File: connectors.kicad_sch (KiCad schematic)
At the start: 2 parts

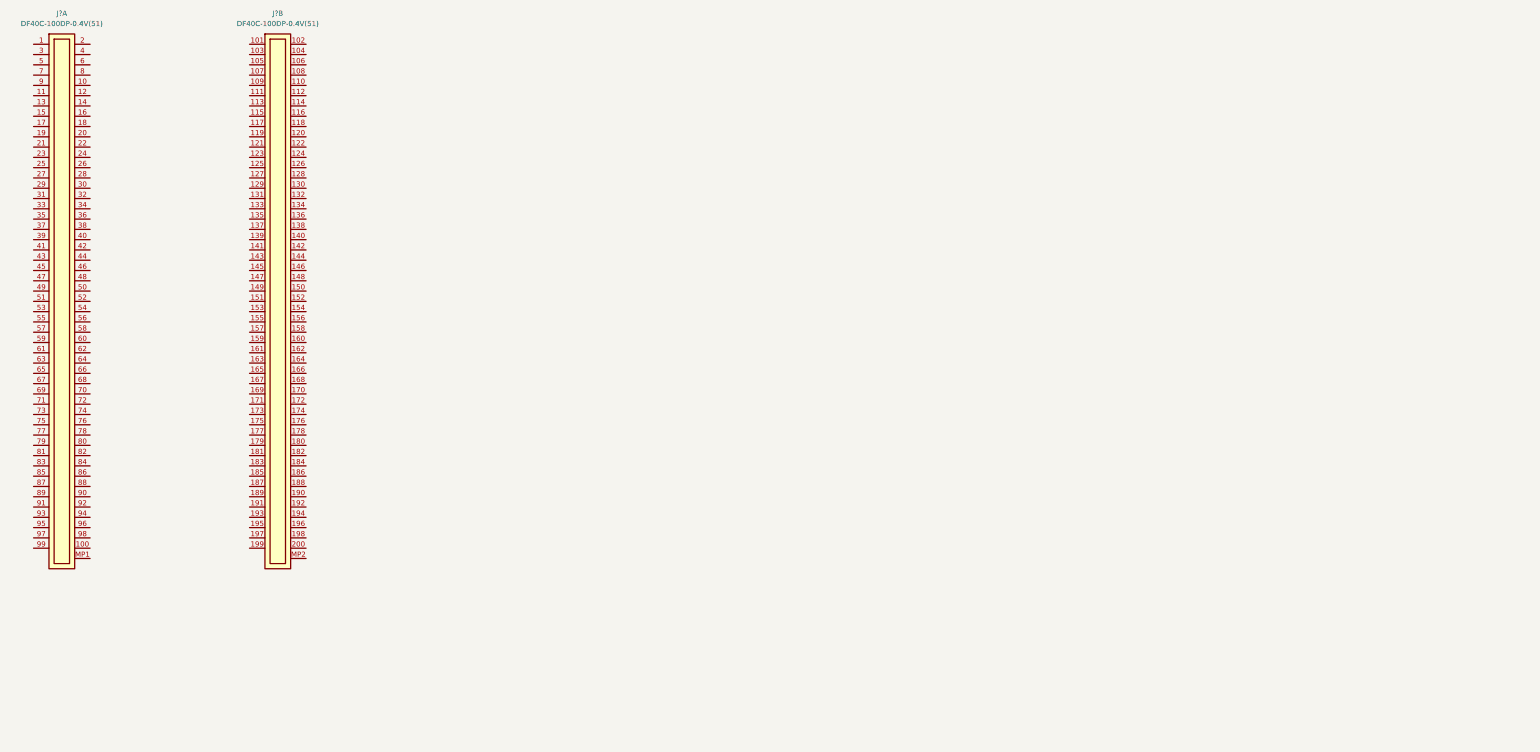
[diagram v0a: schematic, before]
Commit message: [#52579] Connect signals to SoC
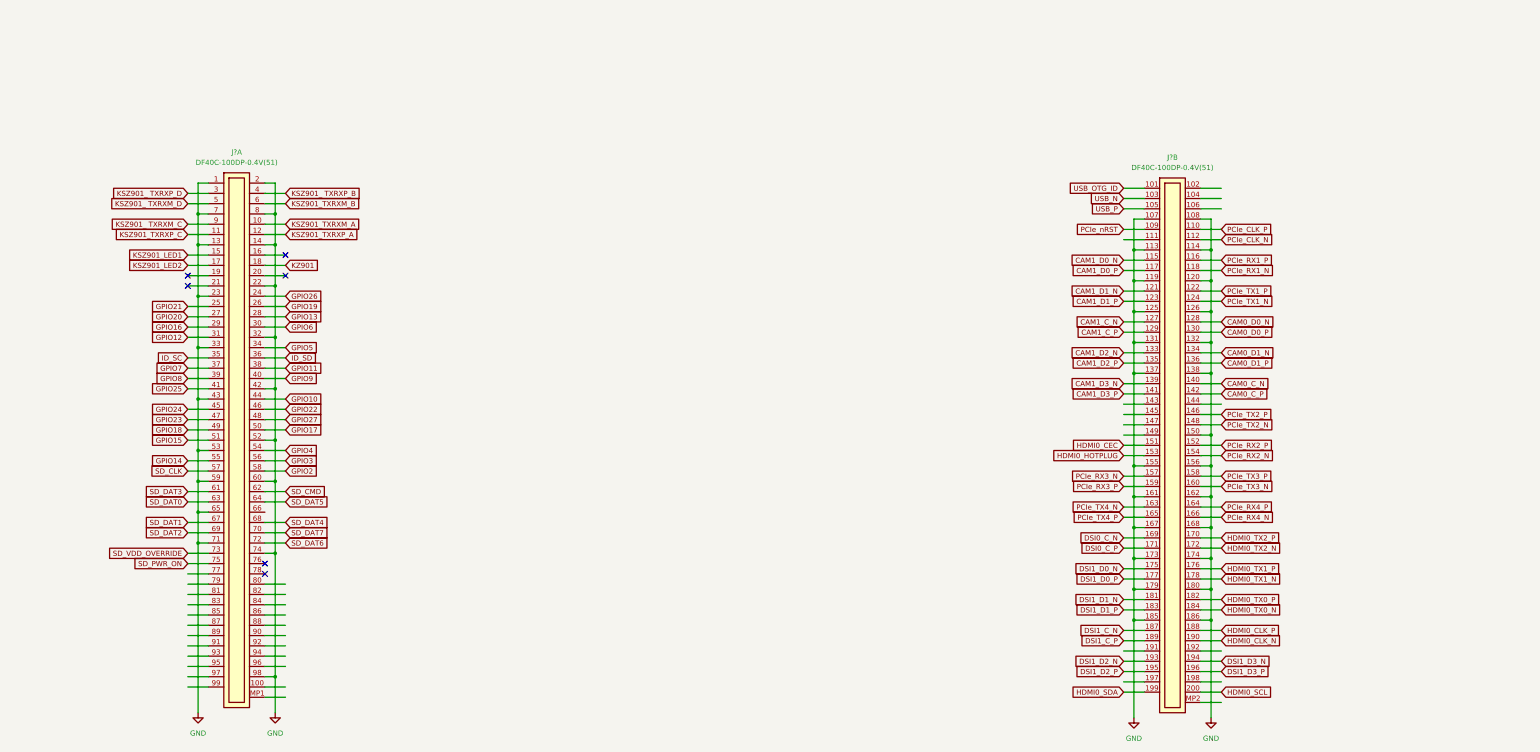
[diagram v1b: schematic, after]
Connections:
- net USB_OTG_ID: now reaches J?.101
- net USB_N: now reaches J?.103
- net USB_P: now reaches J?.105
- net GND: now reaches J?.107
- net GND: now also J?.1, J?.108, J?.113, J?.114, J?.119, J?.120, J?.125, J?.126, J?.13, J?.131, J?.132, J?.137, J?.138, J?.14, J?.150, J?.155, J?.156, J?.161, J?.162, J?.167, J?.168, J?.173, J?.174, J?.179, J?.180, J?.185, J?.186, J?.2, J?.22, J?.23, J?.32, J?.33, J?.42, J?.43, J?.52, J?.53, J?.59, J?.60, J?.65, J?.7, J?.71, J?.74, J?.8, J?.98
- net PCIe_nRST: now reaches J?.109
- net PCIe_CLK_P: now reaches J?.110
- net PCIe_CLK_N: now reaches J?.112
- net CAM1_D0_N: now reaches J?.115
- net PCIe_RX1_P: now reaches J?.116
- net CAM1_D0_P: now reaches J?.117
- net PCIe_RX1_N: now reaches J?.118
- net CAM1_D1_N: now reaches J?.121
- net PCIe_TX1_P: now reaches J?.122
- net CAM1_D1_P: now reaches J?.123
- net PCIe_TX1_N: now reaches J?.124
- net CAM1_C_N: now reaches J?.127
- net CAM0_D0_N: now reaches J?.128
- net CAM1_C_P: now reaches J?.129
- net CAM0_D0_P: now reaches J?.130
- net CAM1_D2_N: now reaches J?.133
- net CAM0_D1_N: now reaches J?.134
- net CAM1_D2_P: now reaches J?.135
- net CAM0_D1_P: now reaches J?.136
- net CAM1_D3_N: now reaches J?.139
- net CAM0_C_N: now reaches J?.140
- net CAM1_D3_P: now reaches J?.141
- net CAM0_C_P: now reaches J?.142
- net PCIe_TX2_P: now reaches J?.146
- net PCIe_TX2_N: now reaches J?.148
- net HDMI0_CEC: now reaches J?.151
- net PCIe_RX2_P: now reaches J?.152
- net HDMI0_HOTPLUG: now reaches J?.153
- net PCIe_RX2_N: now reaches J?.154
- net PCIe_RX3_N: now reaches J?.157
- net PCIe_TX3_P: now reaches J?.158
- net PCIe_RX3_P: now reaches J?.159
- net PCIe_TX3_N: now reaches J?.160
- net PCIe_TX4_N: now reaches J?.163
- net PCIe_RX4_P: now reaches J?.164
- net PCIe_TX4_P: now reaches J?.165
- net PCIe_RX4_N: now reaches J?.166
- net DSI0_C_N: now reaches J?.169
- net HDMI0_TX2_P: now reaches J?.170
- net DSI0_C_P: now reaches J?.171
- net HDMI0_TX2_N: now reaches J?.172
- net DSI1_D0_N: now reaches J?.175
- net HDMI0_TX1_P: now reaches J?.176
- net DSI1_D0_P: now reaches J?.177
- net HDMI0_TX1_N: now reaches J?.178
- net DSI1_D1_N: now reaches J?.181
- net HDMI0_TX0_P: now reaches J?.182
- net DSI1_D1_P: now reaches J?.183
- net HDMI0_TX0_N: now reaches J?.184
- net DSI1_C_N: now reaches J?.187
- net HDMI0_CLK_P: now reaches J?.188
- net DSI1_C_P: now reaches J?.189
- net HDMI0_CLK_N: now reaches J?.190
- net DSI1_D2_N: now reaches J?.193
- net DSI1_D3_N: now reaches J?.194
- net DSI1_D2_P: now reaches J?.195
- net DSI1_D3_P: now reaches J?.196
- net HDMI0_SDA: now reaches J?.199
- net HDMI0_SCL: now reaches J?.200
- net KSZ901_TXRXM_A: now reaches J?.10
- net KSZ901_TXRXP_C: now reaches J?.11
- net KSZ901_TXRXP_A: now reaches J?.12
- net KSZ901_LED1: now reaches J?.15
- net KSZ901_LED2: now reaches J?.17
- net KZ901: now reaches J?.18
- net GPIO26: now reaches J?.24
- net GPIO21: now reaches J?.25
- net GPIO19: now reaches J?.26
- net GPIO20: now reaches J?.27
- net GPIO13: now reaches J?.28
- net GPIO16: now reaches J?.29
- net KSZ901_ TXRXP_D: now reaches J?.3
- net GPIO6: now reaches J?.30
- net GPIO12: now reaches J?.31
- net GPIO5: now reaches J?.34
- net ID_SC: now reaches J?.35
- net ID_SD: now reaches J?.36
- net GPIO7: now reaches J?.37
- net GPIO11: now reaches J?.38
- net GPIO8: now reaches J?.39
- net KSZ901_ TXRXP_B: now reaches J?.4
- net GPIO9: now reaches J?.40
- net GPIO25: now reaches J?.41
- net GPIO10: now reaches J?.44
- net GPIO24: now reaches J?.45
- net GPIO22: now reaches J?.46
- net GPIO23: now reaches J?.47
- net GPIO27: now reaches J?.48
- net GPIO18: now reaches J?.49
- net KSZ901_ TXRXM_D: now reaches J?.5
- net GPIO17: now reaches J?.50
- net GPIO15: now reaches J?.51
- net GPIO4: now reaches J?.54
- net GPIO14: now reaches J?.55
- net GPIO3: now reaches J?.56
- net SD_CLK: now reaches J?.57
- net GPIO2: now reaches J?.58
- net KSZ901_TXRXM_B: now reaches J?.6
- net SD_DAT3: now reaches J?.61
- net SD_CMD: now reaches J?.62
- net SD_DAT0: now reaches J?.63
- net SD_DAT5: now reaches J?.64
- net SD_DAT1: now reaches J?.67
- net SD_DAT4: now reaches J?.68
- net SD_DAT2: now reaches J?.69
- net SD_DAT7: now reaches J?.70
- net SD_DAT6: now reaches J?.72
- net SD_VDD_OVERRIDE: now reaches J?.73
- net SD_PWR_ON: now reaches J?.75
- net KSZ901_ TXRXM_C: now reaches J?.9
- no-connect marks 0 -> 6
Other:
- moved on the sheet: J?A, J?B

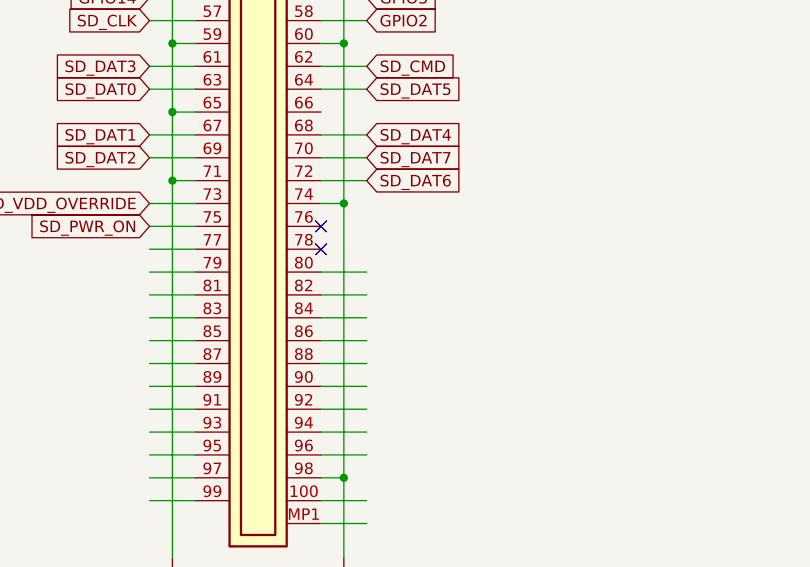
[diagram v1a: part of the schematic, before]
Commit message: [#52579] Add JTAG and connect it to SoC
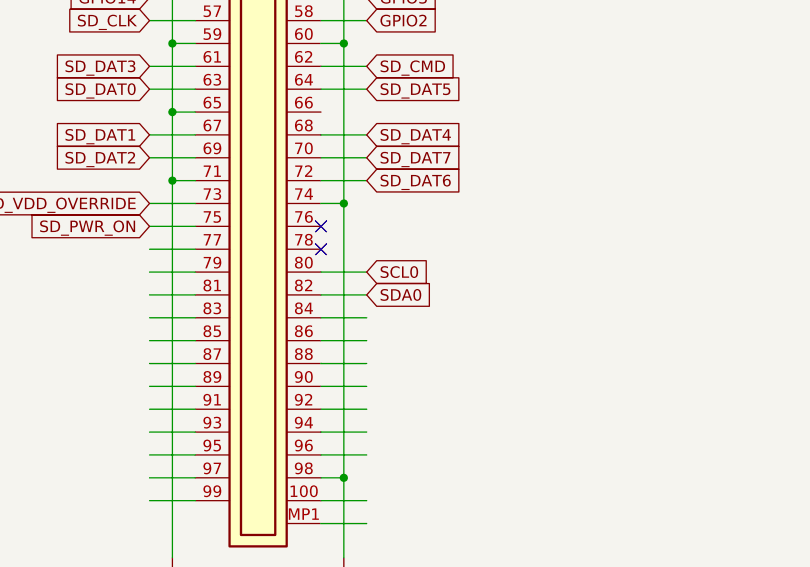
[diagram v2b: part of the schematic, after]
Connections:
- net SCL0: now reaches J?.80
- net SDA0: now reaches J?.82
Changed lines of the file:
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@@
+    )
+  )
+  (global_label "SCL0" (shape input) (at 99.06 179.07 0) (fields_autoplaced)
+    (effects (font (size 1.27 1.27)) (justify left))
+    (property "Intersheet References" "${INTERSHEET_REFS}" (id 0) (at 106.1902 178.9906 0)
+      (effects (font (size 1.27 1.27)) (justify left) hide)
     )
   )
@@
     )
   )
+  (global_label "SDA0" (shape input) (at 99.06 181.61 0) (fields_autoplaced)
+    (effects (font (size 1.27 1.27)) (justify left))
+    (property "Intersheet References" "${INTERSHEET_REFS}" (id 0) (at 106.2507 181.5306 0)
+      (effects (font (size 1.27 1.27)) (justify left) hide)
+    )
+  )

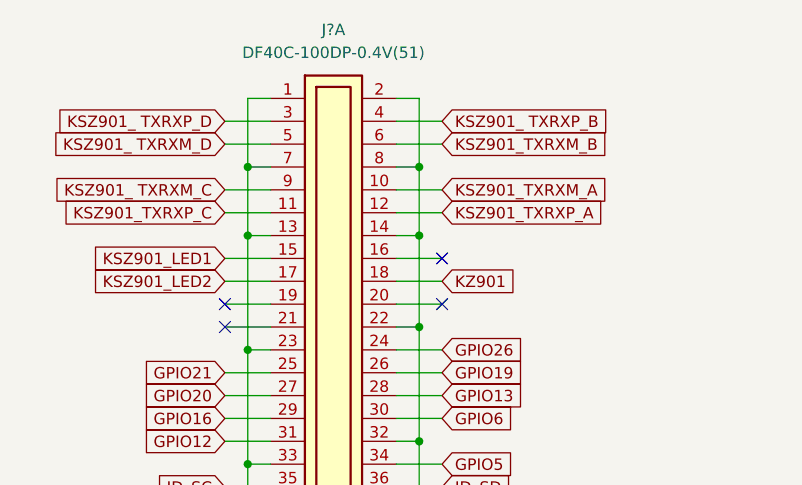
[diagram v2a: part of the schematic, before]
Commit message: [#52579] Add and connect SPI FLASH
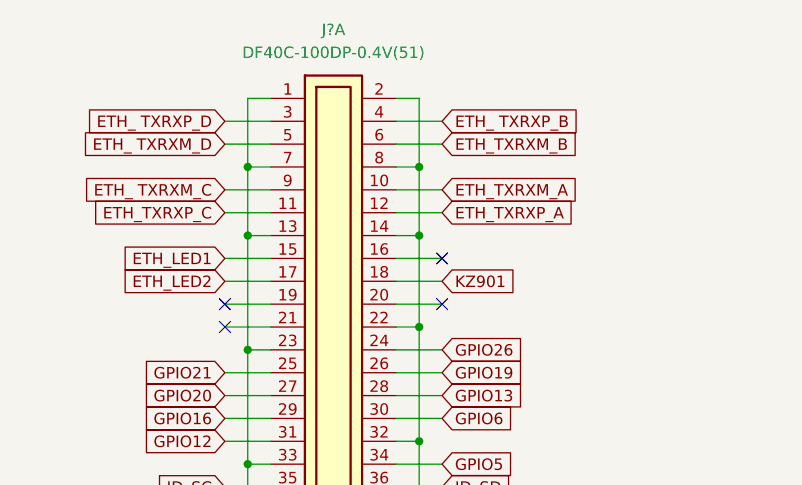
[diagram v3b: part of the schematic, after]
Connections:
- net KSZ901_ TXRXM_C renamed ETH_ TXRXM_C
- net KSZ901_ TXRXM_D renamed ETH_ TXRXM_D
- net KSZ901_ TXRXP_B renamed ETH_ TXRXP_B
- net KSZ901_ TXRXP_D renamed ETH_ TXRXP_D
- net KSZ901_LED1 renamed ETH_LED1
- net KSZ901_LED2 renamed ETH_LED2
- net KSZ901_TXRXM_A renamed ETH_TXRXM_A
- net KSZ901_TXRXM_B renamed ETH_TXRXM_B
- net KSZ901_TXRXP_A renamed ETH_TXRXP_A
- net KSZ901_TXRXP_C renamed ETH_TXRXP_C
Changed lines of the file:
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@@
+    )
+  )
+  (global_label "ETH_TXRXM_B" (shape input) (at 99.06 85.09 0) (fields_autoplaced)
+    (effects (font (size 1.27 1.27)) (justify left))
+    (property "Intersheet References" "${INTERSHEET_REFS}" (id 0) (at 114.2336 85.0106 0)
+      (effects (font (size 1.27 1.27)) (justify left) hide)
     )
   )
@@
     )
   )
-  (global_label "KSZ901_TXRXP_C" (shape input) (at 74.93 92.71 180) (fields_autoplaced)
-    (effects (font (size 1.27 1.27)) (justify right))
-    (property "Intersheet References" "${INTERSHEET_REFS}" (id 0) (at 56.0674 92.6306 0)
-      (effects (font (size 1.27 1.27)) (justify right) hide)
-    )
-  )
   (global_label "PCIe_TX4_P" (shape input) (at 306.07 162.56 180) (fields_autoplaced)
     (effects (font (size 1.27 1.27)) (justify right))
@@
     )
   )
-  (global_label "KSZ901_ TXRXP_D" (shape input) (at 74.93 82.55 180) (fields_autoplaced)
-    (effects (font (size 1.27 1.27)) (justify right))
-    (property "Intersheet References" "${INTERSHEET_REFS}" (id 0) (at 55.0998 82.4706 0)
-      (effects (font (size 1.27 1.27)) (justify right) hide)
+  (global_label "ETH_TXRXM_A" (shape input) (at 99.06 90.17 0) (fields_autoplaced)
+    (effects (font (size 1.27 1.27)) (justify left))
+    (property "Intersheet References" "${INTERSHEET_REFS}" (id 0) (at 114.0521 90.0906 0)
+      (effects (font (size 1.27 1.27)) (justify left) hide)
     )
   )
@@
     )
   )
+  (global_label "ETH_TXRXP_C" (shape input) (at 74.93 92.71 180) (fields_autoplaced)
+    (effects (font (size 1.27 1.27)) (justify right))
+    (property "Intersheet References" "${INTERSHEET_REFS}" (id 0) (at 59.9379 92.6306 0)
+      (effects (font (size 1.27 1.27)) (justify right) hide)
+    )
+  )
   (global_label "PCIe_TX1_P" (shape input) (at 330.2 106.68 0) (fields_autoplaced)
     (effects (font (size 1.27 1.27)) (justify left))
@@
     )
   )
+  (global_label "ETH_LED2" (shape input) (at 74.93 100.33 180) (fields_autoplaced)
+    (effects (font (size 1.27 1.27)) (justify right))
+    (property "Intersheet References" "${INTERSHEET_REFS}" (id 0) (at 63.4455 100.2506 0)
+      (effects (font (size 1.27 1.27)) (justify right) hide)
+    )
+  )
   (global_label "CAM1_D1_P" (shape input) (at 306.07 109.22 180) (fields_autoplaced)
     (effects (font (size 1.27 1.27)) (justify right))
@@
     )
   )
+  (global_label "ETH_ TXRXP_D" (shape input) (at 74.93 82.55 180) (fields_autoplaced)
+    (effects (font (size 1.27 1.27)) (justify right))
+    (property "Intersheet References" "${INTERSHEET_REFS}" (id 0) (at 58.9702 82.4706 0)
+      (effects (font (size 1.27 1.27)) (justify right) hide)
+    )
+  )
   (global_label "GPIO25" (shape input) (at 74.93 130.81 180) (fields_autoplaced)
     (effects (font (size 1.27 1.27)) (justify right))
@@
     )
   )
-  (global_label "KSZ901_LED1" (shape input) (at 74.93 97.79 180) (fields_autoplaced)
-    (effects (font (size 1.27 1.27)) (justify right))
-    (property "Intersheet References" "${INTERSHEET_REFS}" (id 0) (at 59.575 97.7106 0)
-      (effects (font (size 1.27 1.27)) (justify right) hide)
-    )
-  )
-  (global_label "KSZ901_TXRXP_A" (shape input) (at 99.06 92.71 0) (fields_autoplaced)
-    (effects (font (size 1.27 1.27)) (justify left))
-    (property "Intersheet References" "${INTERSHEET_REFS}" (id 0) (at 117.7412 92.6306 0)
-      (effects (font (size 1.27 1.27)) (justify left) hide)
-    )
-  )
   (global_label "CAM0_C_P" (shape input) (at 330.2 132.08 0) (fields_autoplaced)
     (effects (font (size 1.27 1.27)) (justify left))
@@
     )
   )
-  (global_label "KSZ901_ TXRXM_C" (shape input) (at 74.93 90.17 180) (fields_autoplaced)
-    (effects (font (size 1.27 1.27)) (justify right))
-    (property "Intersheet References" "${INTERSHEET_REFS}" (id 0) (at 54.9183 90.0906 0)
-      (effects (font (size 1.27 1.27)) (justify right) hide)
-    )
-  )
   (global_label "SD_DAT3" (shape input) (at 74.93 156.21 180) (fields_autoplaced)
     (effects (font (size 1.27 1.27)) (justify right))
@@
     )
   )
-  (global_label "KSZ901_TXRXM_A" (shape input) (at 99.06 90.17 0) (fields_autoplaced)
-    (effects (font (size 1.27 1.27)) (justify left))
-    (property "Intersheet References" "${INTERSHEET_REFS}" (id 0) (at 117.9226 90.0906 0)
-      (effects (font (size 1.27 1.27)) (justify left) hide)
-    )
-  )
   (global_label "DSI0_C_P" (shape input) (at 306.07 170.18 180) (fields_autoplaced)
     (effects (font (size 1.27 1.27)) (justify right))
@@
     )
   )
-  (global_label "KSZ901_LED2" (shape input) (at 74.93 100.33 180) (fields_autoplaced)
-    (effects (font (size 1.27 1.27)) (justify right))
-    (property "Intersheet References" "${INTERSHEET_REFS}" (id 0) (at 59.575 100.2506 0)
-      (effects (font (size 1.27 1.27)) (justify right) hide)
-    )
-  )
-  (global_label "KSZ901_ TXRXP_B" (shape input) (at 99.06 82.55 0) (fields_autoplaced)
-    (effects (font (size 1.27 1.27)) (justify left))
-    (property "Intersheet References" "${INTERSHEET_REFS}" (id 0) (at 118.8902 82.4706 0)
-      (effects (font (size 1.27 1.27)) (justify left) hide)
-    )
-  )
   (global_label "PCIe_RX2_N" (shape input) (at 330.2 147.32 0) (fields_autoplaced)
     (effects (font (size 1.27 1.27)) (justify left))
@@
     )
   )
-  (global_label "KSZ901_ TXRXM_D" (shape input) (at 74.93 85.09 180) (fields_autoplaced)
-    (effects (font (size 1.27 1.27)) (justify right))
-    (property "Intersheet References" "${INTERSHEET_REFS}" (id 0) (at 54.9183 85.0106 0)
-      (effects (font (size 1.27 1.27)) (justify right) hide)
-    )
-  )
   (global_label "CAM0_C_N" (shape input) (at 330.2 129.54 0) (fields_autoplaced)
     (effects (font (size 1.27 1.27)) (justify left))
@@
     )
   )
+  (global_label "ETH_ TXRXM_D" (shape input) (at 74.93 85.09 180) (fields_autoplaced)
+    (effects (font (size 1.27 1.27)) (justify right))
+    (property "Intersheet References" "${INTERSHEET_REFS}" (id 0) (at 58.7888 85.0106 0)
+      (effects (font (size 1.27 1.27)) (justify right) hide)
+    )
+  )
   (global_label "CAM0_D1_P" (shape input) (at 330.2 124.46 0) (fields_autoplaced)
     (effects (font (size 1.27 1.27)) (justify left))
@@
     )
   )
-  (global_label "KSZ901_TXRXM_B" (shape input) (at 99.06 85.09 0) (fields_autoplaced)
-    (effects (font (size 1.27 1.27)) (justify left))
-    (property "Intersheet References" "${INTERSHEET_REFS}" (id 0) (at 118.1041 85.0106 0)
-      (effects (font (size 1.27 1.27)) (justify left) hide)
+  (global_label "ETH_TXRXP_A" (shape input) (at 99.06 92.71 0) (fields_autoplaced)
+    (effects (font (size 1.27 1.27)) (justify left))
+    (property "Intersheet References" "${INTERSHEET_REFS}" (id 0) (at 113.8707 92.6306 0)
+      (effects (font (size 1.27 1.27)) (justify left) hide)
+    )
+  )
+  (global_label "ETH_ TXRXM_C" (shape input) (at 74.93 90.17 180) (fields_autoplaced)
+    (effects (font (size 1.27 1.27)) (justify right))
+    (property "Intersheet References" "${INTERSHEET_REFS}" (id 0) (at 58.7888 90.0906 0)
+      (effects (font (size 1.27 1.27)) (justify right) hide)
     )
   )
@@
     )
   )
+  (global_label "ETH_LED1" (shape input) (at 74.93 97.79 180) (fields_autoplaced)
+    (effects (font (size 1.27 1.27)) (justify right))
+    (property "Intersheet References" "${INTERSHEET_REFS}" (id 0) (at 63.4455 97.7106 0)
+      (effects (font (size 1.27 1.27)) (justify right) hide)
+    )
+  )
+  (global_label "ETH_ TXRXP_B" (shape input) (at 99.06 82.55 0) (fields_autoplaced)
+    (effects (font (size 1.27 1.27)) (justify left))
+    (property "Intersheet References" "${INTERSHEET_REFS}" (id 0) (at 115.0198 82.4706 0)
+      (effects (font (size 1.27 1.27)) (justify left) hide)
+    )
+  )
